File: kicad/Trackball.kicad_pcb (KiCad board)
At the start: 2 copper layers, 44 x 44 mm, 40 parts, among them J1 Conn_01x04, J2 Conn_02x10_Odd_Even, SW1 SW_Push, SW2 SW_Push, U1 TCR2EF19, U2 PMW3360, U3 RP2040, U4 TLV73333PDBV, U5 W25Q128JVS, Y1 Crystal_GND24

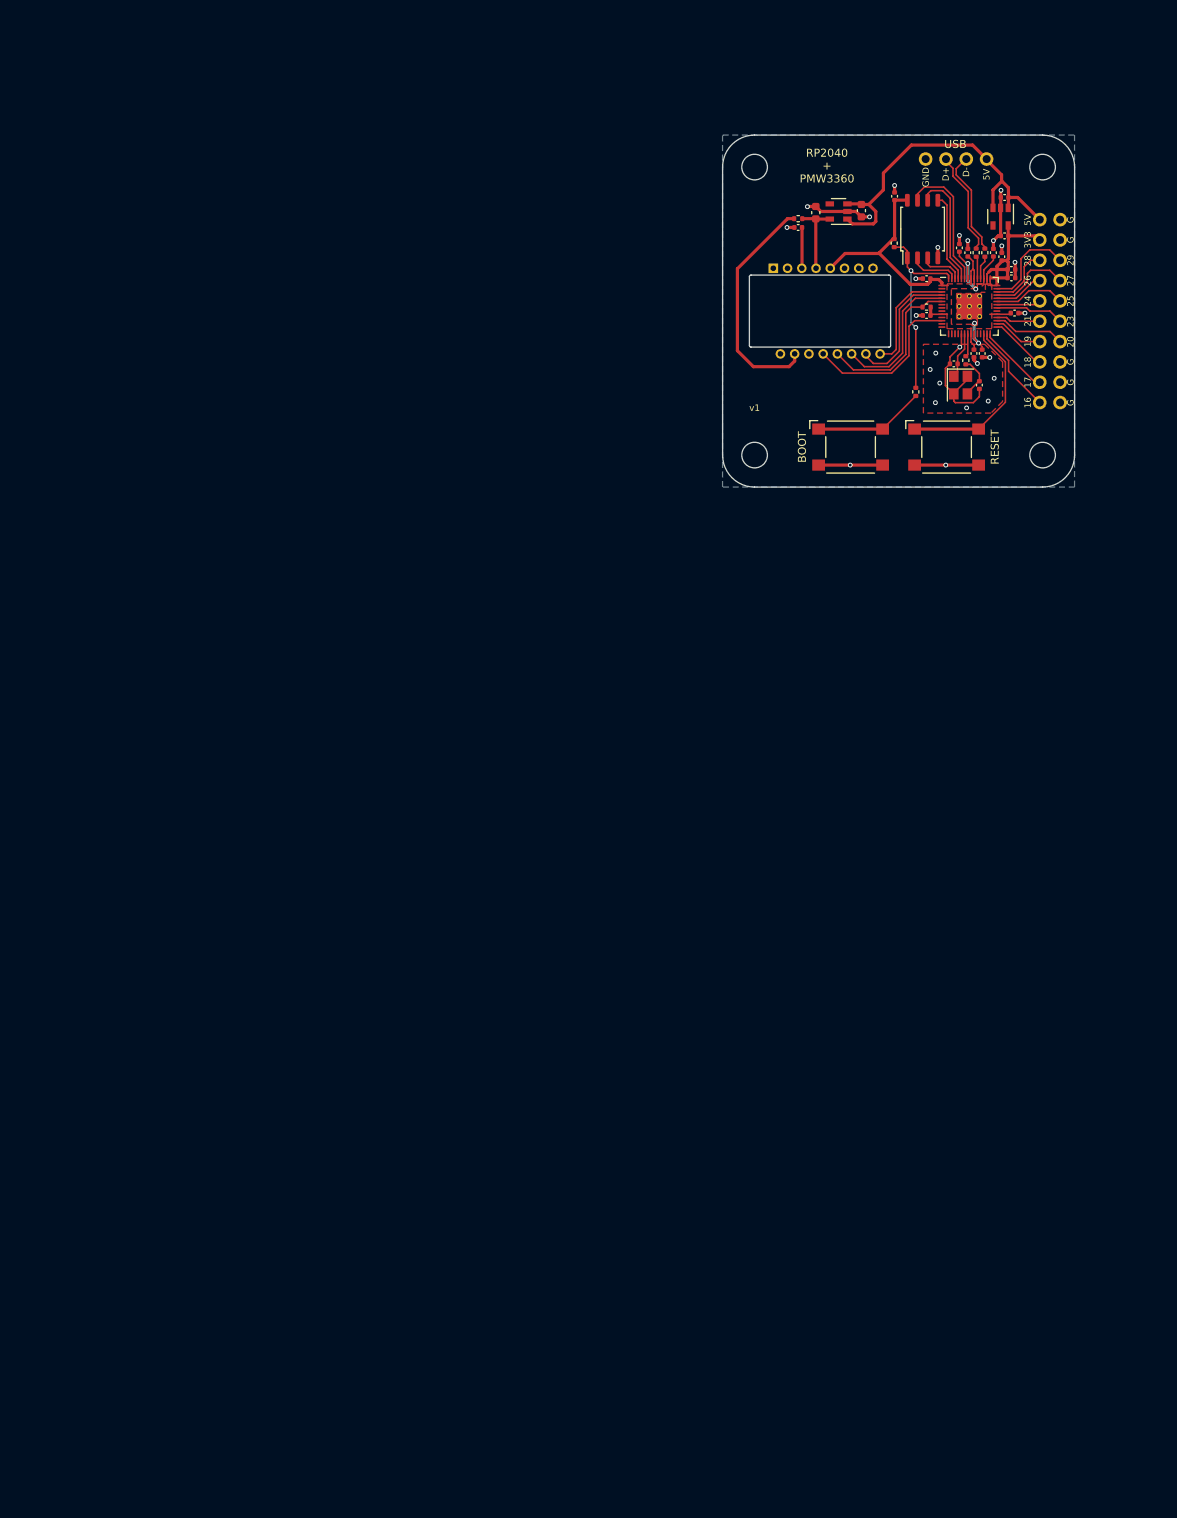
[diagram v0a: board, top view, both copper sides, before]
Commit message: add initial keyboard schematics and pcb
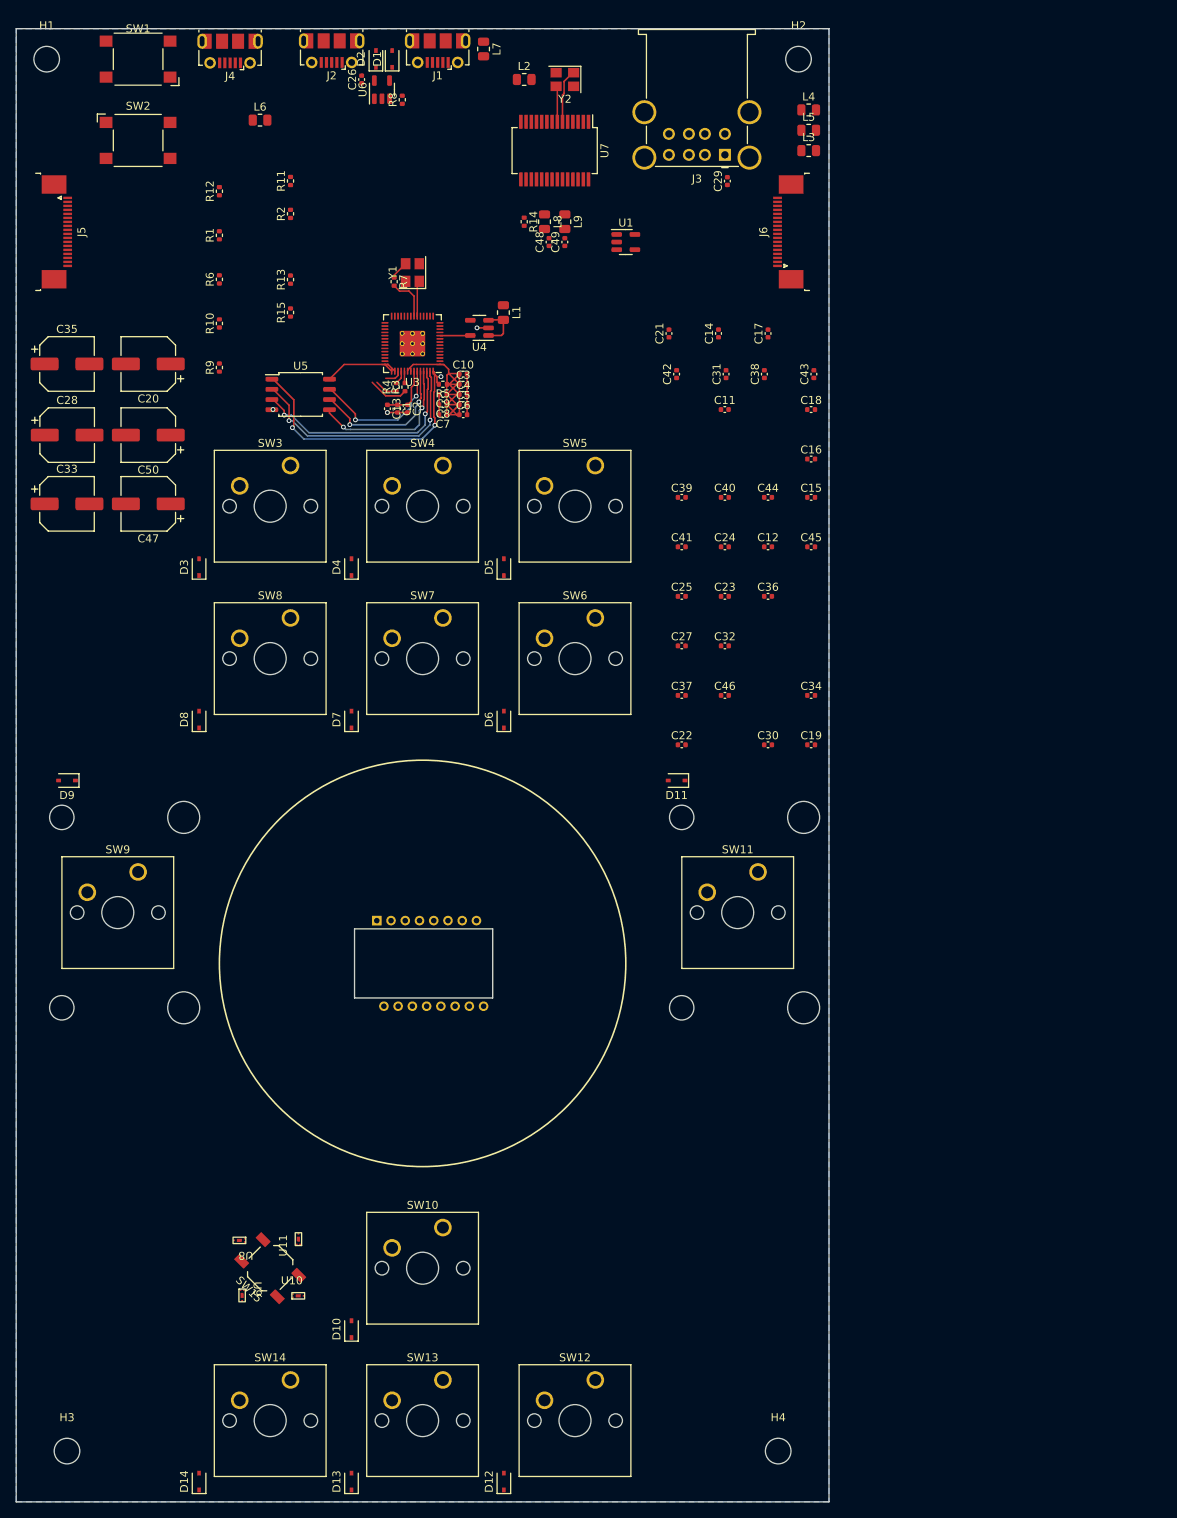
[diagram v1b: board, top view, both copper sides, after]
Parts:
- added C20: 100uF/16V/LOWESR/105C, Capacitor_SMD:CP_Elec_6.3x5.9, F.Cu at (29.2, 54.6)
- added C21: 0.1uF, Capacitor_SMD:C_0402_1005Metric, F.Cu at (94.3, 50.8)
- added C22: 100nF, Capacitor_SMD:C_0402_1005Metric, F.Cu at (95.9, 102.2)
- added C23: 10uF/6.3V, Capacitor_SMD:C_0402_1005Metric, F.Cu at (101.3, 83.7)
- added C24: 100nF, Capacitor_SMD:C_0402_1005Metric, F.Cu at (101.3, 77.5)
- added C25: 100nF, Capacitor_SMD:C_0402_1005Metric, F.Cu at (95.9, 83.7)
- added C26: 10uF/6.3V, Capacitor_SMD:C_0402_1005Metric, F.Cu at (55.9, 19.1)
- added C27: 100nF, Capacitor_SMD:C_0402_1005Metric, F.Cu at (95.9, 89.9)
- added C28: 100uF/16V/LOWESR/105C, Capacitor_SMD:CP_Elec_6.3x5.9, F.Cu at (19.1, 63.5)
- added C29: 0.1uF, Capacitor_SMD:C_0402_1005Metric, F.Cu at (101.6, 31.8)
- added C30: 33pF, Capacitor_SMD:C_0402_1005Metric, F.Cu at (106.7, 102.2)
- added C31: 33pF, Capacitor_SMD:C_0402_1005Metric, F.Cu at (101.4, 55.9)
- added C32: 1uF, Capacitor_SMD:C_0402_1005Metric, F.Cu at (101.3, 89.9)
- added C33: 100uF/16V/LOWESR/105C, Capacitor_SMD:CP_Elec_6.3x5.9, F.Cu at (19.1, 72.1)
- added C34: 0.1uF, Capacitor_SMD:C_0402_1005Metric, F.Cu at (112.1, 96.0)
- added C35: 100uF/16V/LOWESR/105C, Capacitor_SMD:CP_Elec_6.3x5.9, F.Cu at (19.1, 54.6)
- added C36: 0.1uF, Capacitor_SMD:C_0402_1005Metric, F.Cu at (106.7, 83.7)
- added C37: 10uF/6.3V, Capacitor_SMD:C_0402_1005Metric, F.Cu at (95.9, 96.0)
- added C38: 100nF, Capacitor_SMD:C_0402_1005Metric, F.Cu at (106.2, 55.9)
- added C39: 1nF, Capacitor_SMD:C_0402_1005Metric, F.Cu at (95.9, 71.3)
- added C40: 100nF, Capacitor_SMD:C_0402_1005Metric, F.Cu at (101.3, 71.3)
- added C41: 100nF, Capacitor_SMD:C_0402_1005Metric, F.Cu at (95.9, 77.5)
- added C42: 1nF, Capacitor_SMD:C_0402_1005Metric, F.Cu at (95.2, 55.9)
- added C43: 100nF, Capacitor_SMD:C_0402_1005Metric, F.Cu at (112.4, 55.9)
- added C44: 100nF, Capacitor_SMD:C_0402_1005Metric, F.Cu at (106.7, 71.3)
- added C45: 1nF, Capacitor_SMD:C_0402_1005Metric, F.Cu at (112.1, 77.5)
- added C46: 1nF, Capacitor_SMD:C_0402_1005Metric, F.Cu at (101.3, 96.0)
- added C47: 100uF/16V/LOWESR/105C, Capacitor_SMD:CP_Elec_6.3x5.9, F.Cu at (29.2, 72.1)
- added C48: 0.1uF, Capacitor_SMD:C_0402_1005Metric, F.Cu at (79.3, 39.4)
- added C49: 0.1uF, Capacitor_SMD:C_0402_1005Metric, F.Cu at (81.3, 39.4)
- added C50: 100uF/16V/LOWESR/105C, Capacitor_SMD:CP_Elec_6.3x5.9, F.Cu at (29.2, 63.5)
- added D1: D, Diode_SMD:D_SOD-323, F.Cu at (59.7, 16.5)
- added D10: 1N4148W, Diode_SMD:D_SOD-323, F.Cu at (54.6, 175.3)
- added D11: 1N4148W, Diode_SMD:D_SOD-323, F.Cu at (95.2, 106.7)
- added D12: 1N4148W, Diode_SMD:D_SOD-323, F.Cu at (73.7, 194.3)
- added D13: 1N4148W, Diode_SMD:D_SOD-323, F.Cu at (54.6, 194.3)
- added D14: 1N4148W, Diode_SMD:D_SOD-323, F.Cu at (35.6, 194.3)
- added D2: D, Diode_SMD:D_SOD-323, F.Cu at (57.7, 16.5)
- added D3: 1N4148W, Diode_SMD:D_SOD-323, F.Cu at (35.6, 80.0)
- added D4: 1N4148W, Diode_SMD:D_SOD-323, F.Cu at (54.6, 80.0)
- added D5: 1N4148W, Diode_SMD:D_SOD-323, F.Cu at (73.7, 80.0)
- added D6: 1N4148W, Diode_SMD:D_SOD-323, F.Cu at (73.7, 99.1)
- added D7: 1N4148W, Diode_SMD:D_SOD-323, F.Cu at (54.6, 99.1)
- added D8: 1N4148W, Diode_SMD:D_SOD-323, F.Cu at (35.6, 99.1)
- added D9: 1N4148W, Diode_SMD:D_SOD-323, F.Cu at (19.1, 106.7)
- added J3: A2OTG, Connector_USB:USB_A_Wuerth_61400826021_Horizontal_Stacked, F.Cu at (101.3, 28.5)
- added J4: MOTG, Connector_USB:USB_Micro-B_Molex-105017-0001, F.Cu at (39.4, 15.5)
- added J5: FFC LEFT, Connector_FFC-FPC:TE_1-1734839-8_1x18-1MP_P0.5mm_Horizontal, F.Cu at (17.8, 38.1)
- added J6: FFC RIGHT, Connector_FFC-FPC:TE_1-1734839-8_1x18-1MP_P0.5mm_Horizontal, F.Cu at (109.2, 38.1)
- added L1: 600R/2A, Resistor_SMD:R_0805_2012Metric, F.Cu at (73.6, 48.2)
- added L2: 600R/2A, Resistor_SMD:R_0805_2012Metric, F.Cu at (76.2, 19.1)
- added L3: 600R/2A, Resistor_SMD:R_0805_2012Metric, F.Cu at (111.8, 27.9)
- added L4: 600R/2A, Resistor_SMD:R_0805_2012Metric, F.Cu at (111.8, 22.9)
- added L5: 600R/2A, Resistor_SMD:R_0805_2012Metric, F.Cu at (111.8, 25.4)
- added L6: 600R/2A, Resistor_SMD:R_0805_2012Metric, F.Cu at (43.2, 24.1)
- added L7: 600R/200mA, Resistor_SMD:R_0805_2012Metric, F.Cu at (71.1, 15.2)
- added L8: 600R/2A, Resistor_SMD:R_0805_2012Metric, F.Cu at (78.7, 36.8)
- added L9: 600R/2A, Resistor_SMD:R_0805_2012Metric, F.Cu at (81.3, 36.8)
- added R10: 47k, Resistor_SMD:R_0402_1005Metric, F.Cu at (38.1, 49.5)
- added R11: 680R/1%, Resistor_SMD:R_0402_1005Metric, F.Cu at (47.0, 31.7)
- added R12: 47k, Resistor_SMD:R_0402_1005Metric, F.Cu at (38.1, 33.0)
- added R13: 10k, Resistor_SMD:R_0402_1005Metric, F.Cu at (47.0, 44.1)
- added R14: 10k, Resistor_SMD:R_0402_1005Metric, F.Cu at (76.2, 36.8)
- added R15: 5.1k, Resistor_SMD:R_0402_1005Metric, F.Cu at (47.0, 48.2)
- added R8: 4.7k/1%, Resistor_SMD:R_0402_1005Metric, F.Cu at (61.0, 21.6)
- added R9: 10k, Resistor_SMD:R_0402_1005Metric, F.Cu at (38.1, 55.1)
- added SW10: SW_UP, Button_Switch_Keyboard:SW_Cherry_MX_1.00u_PCB, F.Cu at (66.0, 162.6)
- added SW11: SW_RCLK, Button_Switch_Keyboard:SW_Cherry_MX_2.00u_Vertical_PCB, F.Cu at (105.4, 118.1)
- added SW12: SW_RT, Button_Switch_Keyboard:SW_Cherry_MX_1.00u_PCB, F.Cu at (85.1, 181.6)
- added SW13: SW_DN, Button_Switch_Keyboard:SW_Cherry_MX_1.00u_PCB, F.Cu at (66.0, 181.6)
- added SW14: SW_LT, Button_Switch_Keyboard:SW_Cherry_MX_1.00u_PCB, F.Cu at (47.0, 181.6)
- added SW15: MCLK, Button_Switch_SMD:SW_SPST_TL3342, F.Cu at (44.5, 167.6)
- added SW3: SW_INS, Button_Switch_Keyboard:SW_Cherry_MX_1.00u_PCB, F.Cu at (47.0, 67.3)
- added SW4: SW_HOME, Button_Switch_Keyboard:SW_Cherry_MX_1.00u_PCB, F.Cu at (66.0, 67.3)
- added SW5: SW_PGUP, Button_Switch_Keyboard:SW_Cherry_MX_1.00u_PCB, F.Cu at (85.1, 67.3)
- added SW6: SW_PGDN, Button_Switch_Keyboard:SW_Cherry_MX_1.00u_PCB, F.Cu at (85.1, 86.4)
- added SW7: SW_END, Button_Switch_Keyboard:SW_Cherry_MX_1.00u_PCB, F.Cu at (66.0, 86.4)
- added SW8: SW_DEL, Button_Switch_Keyboard:SW_Cherry_MX_1.00u_PCB, F.Cu at (47.0, 86.4)
- added SW9: SW_LCLK, Button_Switch_Keyboard:SW_Cherry_MX_2.00u_Vertical_PCB, F.Cu at (27.9, 118.1)
- added U10: DN, RP2040:MT8691DT-1608, F.Cu at (47.2, 170.7)
- added U11: RT, RP2040:MT8691DT-1608, F.Cu at (47.6, 164.8)
- added U6: SY6280, Package_TO_SOT_SMD:SOT-23-5, F.Cu at (58.4, 20.3)
- added U7: GL850G, Package_SO:SSOP-28_5.3x10.2mm_P0.65mm, F.Cu at (80.0, 27.9)
- added U8: UP, RP2040:MT8691DT-1608, F.Cu at (41.4, 164.6)
- added U9: LT, RP2040:MT8691DT-1608, F.Cu at (41.3, 170.2)
- added Y2: 12Mhz, Crystal:Crystal_SMD_3225-4Pin_3.2x2.5mm, F.Cu at (81.3, 19.1)
- C11, C12: footprint Capacitor_SMD:C_0603_1608Metric -> Capacitor_SMD:C_0402_1005Metric
- J1: value Conn_01x04 -> MDIN; footprint Connector_PinHeader_2.54mm:PinHeader_1x04_P2.54mm_Vertical -> Connector_USB:USB_Micro-B_Molex-105017-0001
- J2: value Conn_02x10_Odd_Even -> MPIN; footprint Connector_PinHeader_2.54mm:PinHeader_2x10_P2.54mm_Vertical -> Connector_USB:USB_Micro-B_Molex-105017-0001
- SW1: value SW_Push -> RUN
- SW2: value SW_Push -> FLASH
- Y1: value Crystal_GND24 -> 12MHz
- moved H3 201.6 mm to (19.1, 190.5)
- moved H4 128.8 mm to (108.0, 190.5)
- moved SW1 112.1 mm to (27.9, 16.5), turned to 180 degrees
- moved SW2 97.0 mm to (27.9, 26.7)
- moved U2 95.4 mm to (57.8, 124.2)
- moved J2 91.0 mm to (52.1, 15.5), turned to 180 degrees
- moved H1 89.5 mm to (16.5, 16.5)
- moved R6 88.2 mm to (38.1, 44.0), turned to 90 degrees
- moved U5 80.4 mm to (48.3, 58.4), turned to 0 degrees
- moved R2 80.4 mm to (47.0, 35.8), turned to 90 degrees
- moved C13 78.2 mm to (59.1, 60.2), turned to -90 degrees
- moved R4 75.5 mm to (60.2, 57.5), turned to 90 degrees
- moved R3 73.4 mm to (61.3, 57.5), turned to 90 degrees
- moved C1 73.0 mm to (60.4, 60.2), turned to -90 degrees
- moved C8 72.8 mm to (66.0, 59.7), turned to 180 degrees
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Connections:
- C11 pad 2: +5V -> Net-(C11-Pad2)
- C15 pad 1: +5V -> Net-(C11-Pad2)
- J1 pad 1: +5V -> /5V-IN-USB
- J1 pad 2: D- -> D0+
- J1 pad 3: D+ -> D0-
- J1 pad 4: GND -> unconnected-(J1-Pad4)
- J2 pad 1: +5V -> Net-(D2-Pad2)
- J2 pad 2: GND -> unconnected-(J2-Pad2)
- J2 pad 3: +3V3 -> unconnected-(J2-Pad3)
- J2 pad 4: GND -> unconnected-(J2-Pad4)
- J2 pad 5: GPIO28 -> GND
- J2 pad 6: GPIO29 -> unconnected-(J2-Pad6)
- R3 pad 1: D+ -> D1+
- R4 pad 1: D- -> D1-
- U1 pad 1: +5V -> Net-(C11-Pad2)
- U1 pad 3: +5V -> Net-(C11-Pad2)
- U1 pad 4: Net-(U1-Pad4) -> unconnected-(U1-Pad4)
- U2 pad 1: Net-(U2-Pad1) -> unconnected-(U2-Pad1)
- U2 pad 14: Net-(U2-Pad14) -> unconnected-(U2-Pad14)
- U2 pad 16: Net-(U2-Pad16) -> unconnected-(U2-Pad16)
- U2 pad 2: Net-(U2-Pad2) -> unconnected-(U2-Pad2)
- U2 pad 6: Net-(U2-Pad6) -> unconnected-(U2-Pad6)
- U2 pad 7: Net-(U2-Pad7) -> unconnected-(U2-Pad7)
- U3 pad 11: Net-(U3-Pad11) -> 08_COL11
- U3 pad 13: Net-(U3-Pad13) -> 10_COL10
- U3 pad 14: Net-(U3-Pad14) -> 14_COL09
- U3 pad 15: Net-(U3-Pad15) -> 12_ROW0
- U3 pad 16: Net-(U3-Pad16) -> 13_ROW1
- U3 pad 17: Net-(U3-Pad17) -> 14_ROW2
- U3 pad 18: Net-(U3-Pad18) -> 15_ROW3
- U3 pad 2: Net-(U3-Pad2) -> 00_COL14
- U3 pad 24: Net-(U3-Pad24) -> unconnected-(U3-Pad24)
- U3 pad 25: Net-(U3-Pad25) -> unconnected-(U3-Pad25)
- U3 pad 27: GPIO16 -> 16_ROW4
- U3 pad 28: GPIO17 -> 17_ROW5
- U3 pad 29: GPIO18 -> 18_COL00
- U3 pad 30: GPIO19 -> 19_COL01
- U3 pad 31: GPIO20 -> 20_COL02
- U3 pad 32: GPIO21 -> 21_COL03
- U3 pad 34: Net-(U3-Pad34) -> 22_COL04
- U3 pad 35: GPIO23 -> 23_COL05
- U3 pad 36: GPIO24 -> GPIO0
- U3 pad 38: GPIO26 -> 26A0_COL06
- U3 pad 39: GPIO27 -> 27A1_COL07
- U3 pad 40: GPIO28 -> 27A2_COL08
- U3 pad 41: GPIO29 -> GPIO29_ADC3
- U3 pad 7: Net-(U3-Pad7) -> 07_COL13
- U3 pad 8: Net-(U3-Pad8) -> 06_COL12
- U3 pad 9: Net-(U3-Pad9) -> 07_COL12
- U4 pad 1: +5V -> Net-(C11-Pad2)
- U4 pad 3: +5V -> Net-(C11-Pad2)
- U4 pad 4: Net-(U4-Pad4) -> unconnected-(U4-Pad4)
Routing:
- net GND: track 61.8 -> 11.7 mm, vias 26 -> 3
- net +5V: track 45.0 -> 0.00 mm
- net Net-(R1-Pad2): track 29.1 -> 0.00 mm
- net QSPI_SD1: track 6.19 -> 30.7 mm, vias 0 -> 2
- net QSPI_SD2: track 5.47 -> 28.6 mm, vias 0 -> 2
- net Net-(SW1-Pad2): track 22.5 -> 0.00 mm
- net NCS: track 20.7 -> 0.00 mm
- net MISO: track 20.5 -> 0.00 mm
- net MOSI: track 18.6 -> 0.00 mm
- net SCLK: track 16.8 -> 0.00 mm
- net MOTION: track 14.0 -> 0.00 mm
- net Net-(R6-Pad2): track 13.9 -> 0.00 mm
- net D-: track 13.2 -> 0.00 mm
- net D+: track 13.0 -> 0.00 mm
- net GPIO29: track 12.0 -> 0.00 mm
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- added copper zone on B.Cu, net 10_COL10
- removed copper zone on F.Cu, net +1V1
- removed copper zone on F.Cu, net +3V3
- removed copper zone on B.Cu, net GND
- removed copper zone on F.Cu, net GND
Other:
- board size 44 x 44 mm -> 101.6 x 184.2 mm
- net class Default removed
- net class Power removed
- net class dPair removed
- board text removed: "16"
- board text removed: "17"
- board text removed: "18"
- board text removed: "19"
- board text removed: "20"
- board text removed: "21"
- board text removed: "23"
- board text removed: "24"
- board text removed: "25"
- board text removed: "26"
- board text removed: "27"
- board text removed: "28"
- board text removed: "29"
- board text removed: "3V3"
- board text removed: "5V"
- board text removed: "BOOT"
- board text removed: "D+"
- board text removed: "D-"
- board text removed: "G"
- board text removed: "GND"
- board text removed: "MISO: GPIO4 MOSI: GPIO3 SCLK: GPIO2 NCS: GPIO9 MOTION: GPIO1"
- board text removed: "RESET"
- board text removed: "RP2040 + PMW3360"
- board text removed: "USB"
- board text removed: "github.com/jfedor2/rp2040-pmw3360"
- board text removed: "v1"

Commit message: progress
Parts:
- moved C20 153.2 mm to (138.5, 161.9), turned to 0 degrees
- moved U1 151.4 mm to (138.5, 182.4)
- moved L1 136.4 mm to (146.0, 163.8), turned to 0 degrees
- moved U4 133.6 mm to (146.4, 160.1), turned to 0 degrees
- moved C11 129.5 mm to (142.5, 183.1)
- moved C21 124.0 mm to (137.4, 167.0), turned to 0 degrees
- moved C12 109.7 mm to (142.5, 181.1)
- moved R1 104.5 mm to (142.5, 33.8)
- moved R10 104.5 mm to (142.5, 44.9)
- moved R11 104.5 mm to (151.4, 27.1)
- moved R15 104.5 mm to (151.4, 43.5)
- moved R2 104.5 mm to (151.4, 31.2)
- moved R6 104.5 mm to (142.5, 39.4)
- moved C16 100.0 mm to (150.4, 158.9)
- moved C15 98.3 mm to (134.6, 167.0)
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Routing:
- net QSPI_SS: track 36.1 -> 10.1 mm, vias 3 -> 0
- net QSPI_SD1: track 30.7 -> 9.90 mm, vias 2 -> 0
- net D3+: track 0.00 -> 20.4 mm, vias 0 -> 2
- net D0-: track 0.00 -> 19.8 mm, vias 0 -> 2
- net D3-: track 0.00 -> 19.7 mm, vias 0 -> 2
- net D2-: track 0.00 -> 19.6 mm
- net /5V-DP: track 0.00 -> 18.9 mm
- net QSPI_SD2: track 28.6 -> 10.3 mm, vias 2 -> 0
- net D0+: track 0.00 -> 18.3 mm
- net D2+: track 0.00 -> 17.4 mm
- net /5V: track 0.00 -> 16.6 mm
- net /V33: track 0.00 -> 12.6 mm, vias 0 -> 2
- net /5V-IN-USB: track 0.00 -> 12.0 mm
- net Net-(C48-Pad2): track 0.00 -> 9.07 mm
- net Net-(J1-Pad6): track 0.00 -> 8.98 mm
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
